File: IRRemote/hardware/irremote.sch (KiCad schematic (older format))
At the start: 35 parts, among them P1 USB_OTG, P2 TL1838_PINHEADER, P3 DS18B20_PINHEADER_TO92, P4 CONN_02X04, P5 CONN_01X04, P6 CONN_01X05, P7 CONN_01X04, P8 TEMP6000, P9 CONN_01X02, Q1 Q_NPN_BEC (MMBT2222ALT1G, 145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

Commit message: IRRemote layout
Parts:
- added R13, R14: 470, Resistors_SMD:R_0805_HandSoldering, symbol R
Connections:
- net RXD_UA_1: now also R14.2; no longer U1.22 (TXD)
- net TXD_UA_1: now also R13.2; no longer U1.21 (RXD)
- net USBDM_1- renamed USBDM_1_N
- net USBDP_1+ renamed USBDP_1_P
- new net: R13.1, U1.21 (RXD)
- new net: R14.1, U1.22 (TXD)
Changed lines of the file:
@@
 $EndComp
 $Comp
-L GND #PWR01
+L GND #PWR13
 U 1 1 58BC3861
 P 5550 4150
-F 0 "#PWR01" H 5550 3900 50  0001 C CNN
+F 0 "#PWR13" H 5550 3900 50  0001 C CNN
 F 1 "GND" H 5550 4000 50  0000 C CNN
 F 2 "" H 5550 4150 50  0000 C CNN
@@
 $EndComp
 $Comp
-L +3.3V #PWR02
+L +3.3V #PWR19
 U 1 1 58BC38AD
 P 6350 3600
-F 0 "#PWR02" H 6350 3450 50  0001 C CNN
+F 0 "#PWR19" H 6350 3450 50  0001 C CNN
 F 1 "+3.3V" H 6350 3740 50  0000 C CNN
 F 2 "" H 6350 3600 50  0000 C CNN
@@
 $EndComp
 $Comp
-L +5V #PWR03
+L +5V #PWR10
 U 1 1 58BC38D1
 P 4600 3600
-F 0 "#PWR03" H 4600 3450 50  0001 C CNN
+F 0 "#PWR10" H 4600 3450 50  0001 C CNN
 F 1 "+5V" H 4600 3740 50  0000 C CNN
 F 2 "" H 4600 3600 50  0000 C CNN
@@
 $EndComp
 $Comp
-L GND #PWR04
+L GND #PWR18
 U 1 1 58BC3BD7
 P 6300 5350
-F 0 "#PWR04" H 6300 5100 50  0001 C CNN
+F 0 "#PWR18" H 6300 5100 50  0001 C CNN
 F 1 "GND" H 6300 5200 50  0000 C CNN
 F 2 "" H 6300 5350 50  0000 C CNN
@@
 $EndComp
 $Comp
-L +5V #PWR05
+L +5V #PWR14
 U 1 1 58BC3BFA
 P 5650 5350
-F 0 "#PWR05" H 5650 5200 50  0001 C CNN
+F 0 "#PWR14" H 5650 5200 50  0001 C CNN
 F 1 "+5V" H 5650 5490 50  0000 C CNN
 F 2 "" H 5650 5350 50  0000 C CNN
@@
 $EndComp
 $Comp
-L GND #PWR06
+L GND #PWR9
 U 1 1 58BC3E12
 P 4550 2600
-F 0 "#PWR06" H 4550 2350 50  0001 C CNN
+F 0 "#PWR9" H 4550 2350 50  0001 C CNN
 F 1 "GND" H 4550 2450 50  0000 C CNN
 F 2 "" H 4550 2600 50  0000 C CNN
@@
 $EndComp
 $Comp
-L +3.3V #PWR07
+L +3.3V #PWR3
 U 1 1 58BC3E35
 P 2000 2500
-F 0 "#PWR07" H 2000 2350 50  0001 C CNN
+F 0 "#PWR3" H 2000 2350 50  0001 C CNN
 F 1 "+3.3V" H 2000 2640 50  0000 C CNN
 F 2 "" H 2000 2500 50  0000 C CNN
@@
 $EndComp
 $Comp
-L GND #PWR08
+L GND #PWR15
 U 1 1 58BC43F9
 P 5950 1700
-F 0 "#PWR08" H 5950 1450 50  0001 C CNN
+F 0 "#PWR15" H 5950 1450 50  0001 C CNN
 F 1 "GND" H 5950 1550 50  0000 C CNN
 F 2 "" H 5950 1700 50  0000 C CNN
@@
 $EndComp
 $Comp
-L +5V #PWR09
+L +5V #PWR24
 U 1 1 58BC455F
 P 7750 2200
-F 0 "#PWR09" H 7750 2050 50  0001 C CNN
+F 0 "#PWR24" H 7750 2050 50  0001 C CNN
 F 1 "+5V" H 7750 2340 50  0000 C CNN
 F 2 "" H 7750 2200 50  0000 C CNN
@@
 LED_DR
 $Comp
-L GND #PWR010
+L GND #PWR20
 U 1 1 58BC492A
 P 7300 3700
-F 0 "#PWR010" H 7300 3450 50  0001 C CNN
+F 0 "#PWR20" H 7300 3450 50  0001 C CNN
 F 1 "GND" H 7300 3550 50  0000 C CNN
 F 2 "" H 7300 3700 50  0000 C CNN
@@
 $EndComp
 $Comp
-L +3.3V #PWR011
+L +3.3V #PWR21
 U 1 1 58BC49D6
 P 7400 3550
-F 0 "#PWR011" H 7400 3400 50  0001 C CNN
+F 0 "#PWR21" H 7400 3400 50  0001 C CNN
 F 1 "+3.3V" H 7400 3690 50  0000 C CNN
 F 2 "" H 7400 3550 50  0000 C CNN
@@
 $EndComp
 $Comp
-L GND #PWR012
+L GND #PWR23
 U 1 1 58BC52F4
 P 7650 5200
-F 0 "#PWR012" H 7650 4950 50  0001 C CNN
+F 0 "#PWR23" H 7650 4950 50  0001 C CNN
 F 1 "GND" H 7650 5050 50  0000 C CNN
 F 2 "" H 7650 5200 50  0000 C CNN
@@
 $EndComp
 $Comp
-L +3.3V #PWR013
+L +3.3V #PWR22
 U 1 1 58BC52FA
 P 7650 4600
-F 0 "#PWR013" H 7650 4450 50  0001 C CNN
+F 0 "#PWR22" H 7650 4450 50  0001 C CNN
 F 1 "+3.3V" H 7650 4740 50  0000 C CNN
 F 2 "" H 7650 4600 50  0000 C CNN
@@
 $EndComp
 $Comp
-L GND #PWR014
+L GND #PWR6
 U 1 1 58C2C51A
 P 3600 5400
-F 0 "#PWR014" H 3600 5150 50  0001 C CNN
+F 0 "#PWR6" H 3600 5150 50  0001 C CNN
 F 1 "GND" H 3600 5250 50  0000 C CNN
 F 2 "" H 3600 5400 50  0000 C CNN
@@
 $EndComp
 Text GLabel 1400 5750 2    60   Input ~ 0
-USBDP_1+
+USBDP_1_P
 Text GLabel 3400 5800 0    60   Input ~ 0
-USBDM_1-
-$Comp
-L +5V #PWR015
+USBDM_1_N
+$Comp
+L +5V #PWR5
 U 1 1 58C2C51D
 P 3300 5250
-F 0 "#PWR015" H 3300 5100 50  0001 C CNN
+F 0 "#PWR5" H 3300 5100 50  0001 C CNN
 F 1 "+5V" H 3300 5390 50  0000 C CNN
 F 2 "" H 3300 5250 50  0000 C CNN
@@
 $EndComp
 $Comp
-L GND #PWR016
+L GND #PWR1
 U 1 1 58C2C51E
 P 1150 5250
-F 0 "#PWR016" H 1150 5000 50  0001 C CNN
+F 0 "#PWR1" H 1150 5000 50  0001 C CNN
 F 1 "GND" H 1150 5100 50  0000 C CNN
 F 2 "" H 1150 5250 50  0000 C CNN
@@
 $EndComp
 Text GLabel 6000 5700 2    60   Input ~ 0
-USBDP_1+
+USBDP_1_P
 Text GLabel 6000 5850 2    60   Input ~ 0
-USBDM_1-
+USBDM_1_N
 Text GLabel 1700 5150 0    60   Input ~ 0
 RXD_UA_1
-Text GLabel 4100 1450 1    60   Input ~ 0
+Text GLabel 4100 1000 1    60   Input ~ 0
 TXD_UA_1
-Text GLabel 4250 1450 1    60   Input ~ 0
+Text GLabel 4250 1000 1    60   Input ~ 0
 RXD_UA_1
 $Comp
@@
 $EndComp
 $Comp
-L +3.3V #PWR017
+L +3.3V #PWR8
 U 1 1 58C2D5B7
 P 4450 5150
-F 0 "#PWR017" H 4450 5000 50  0001 C CNN
+F 0 "#PWR8" H 4450 5000 50  0001 C CNN
 F 1 "+3.3V" H 4450 5290 50  0000 C CNN
 F 2 "" H 4450 5150 50  0000 C CNN
@@
 $EndComp
 $Comp
-L GND #PWR018
+L GND #PWR11
 U 1 1 58C2D60A
 P 4900 5150
-F 0 "#PWR018" H 4900 4900 50  0001 C CNN
+F 0 "#PWR11" H 4900 4900 50  0001 C CNN
 F 1 "GND" H 4900 5000 50  0000 C CNN
 F 2 "" H 4900 5150 50  0000 C CNN
@@
 $EndComp
 $Comp
-L +3.3V #PWR019
+L +3.3V #PWR2
 U 1 1 58C2E848
 P 1650 1600
-F 0 "#PWR019" H 1650 1450 50  0001 C CNN
+F 0 "#PWR2" H 1650 1450 50  0001 C CNN
 F 1 "+3.3V" H 1650 1740 50  0000 C CNN
 F 2 "" H 1650 1600 50  0000 C CNN
@@
 $EndComp
 $Comp
-L GND #PWR020
+L GND #PWR4
 U 1 1 58C2EADC
 P 2900 1050
-F 0 "#PWR020" H 2900 800 50  0001 C CNN
+F 0 "#PWR4" H 2900 800 50  0001 C CNN
 F 1 "GND" H 2900 900 50  0000 C CNN
 F 2 "" H 2900 1050 50  0000 C CNN
@@
 $EndComp
 $Comp
-L +3.3V #PWR021
+L +3.3V #PWR12
 U 1 1 58C2FF8D
 P 5300 2350
-F 0 "#PWR021" H 5300 2200 50  0001 C CNN
+F 0 "#PWR12" H 5300 2200 50  0001 C CNN
 F 1 "+3.3V" H 5300 2490 50  0000 C CNN
 F 2 "" H 5300 2350 50  0000 C CNN
@@
 $EndComp
 $Comp
-L GND #PWR022
+L GND #PWR7
 U 1 1 58C3055D
 P 4150 3250
-F 0 "#PWR022" H 4150 3000 50  0001 C CNN
+F 0 "#PWR7" H 4150 3000 50  0001 C CNN
 F 1 "GND" H 4150 3100 50  0000 C CNN
 F 2 "" H 4150 3250 50  0000 C CNN
@@
 $EndComp
 $Comp
-L GND #PWR023
+L GND #PWR16
 U 1 1 58C30AFA
 P 6150 2600
-F 0 "#PWR023" H 6150 2350 50  0001 C CNN
+F 0 "#PWR16" H 6150 2350 50  0001 C CNN
 F 1 "GND" H 6150 2450 50  0000 C CNN
 F 2 "" H 6150 2600 50  0000 C CNN
@@
 $EndComp
 $Comp
-L +3.3V #PWR024
+L +3.3V #PWR17
 U 1 1 58C30B00
 P 6250 2450
-F 0 "#PWR024" H 6250 2300 50  0001 C CNN
+F 0 "#PWR17" H 6250 2300 50  0001 C CNN
 F 1 "+3.3V" H 6250 2590 50  0000 C CNN
 F 2 "" H 6250 2450 50  0000 C CNN
@@
 $EndComp
 $Comp
-L GND #PWR025
+L GND #PWR26
 U 1 1 58C2E738
 P 8650 3950
-F 0 "#PWR025" H 8650 3700 50  0001 C CNN
+F 0 "#PWR26" H 8650 3700 50  0001 C CNN
 F 1 "GND" H 8650 3800 50  0000 C CNN
 F 2 "" H 8650 3950 50  0000 C CNN
@@
 $EndComp
 $Comp
-L +5V #PWR026
+L +5V #PWR25
 U 1 1 58C2E7AC
 P 8650 3650
-F 0 "#PWR026" H 8650 3500 50  0001 C CNN
+F 0 "#PWR25" H 8650 3500 50  0001 C CNN
 F 1 "+5V" H 8650 3790 50  0000 C CNN
 F 2 "" H 8650 3650 50  0000 C CNN
@@
 Wire Wire Line
 	8650 3750 8650 3650
+$Comp
+L R R13
+U 1 1 58C4A727
+P 4100 1300
+F 0 "R13" V 4180 1300 50  0000 C CNN
+F 1 "470" V 4100 1300 50  0000 C CNN
+F 2 "Resistors_SMD:R_0805_HandSoldering" V 4030 1300 50  0001 C CNN
+F 3 "" H 4100 1300 50  0000 C CNN
+	1    4100 1300
+	-1   0    0    1
+$EndComp
+$Comp
+L R R14
+U 1 1 58C4A7E7
+P 4250 1300
+F 0 "R14" V 4330 1300 50  0000 C CNN
+F 1 "470" V 4250 1300 50  0000 C CNN
+F 2 "Resistors_SMD:R_0805_HandSoldering" V 4180 1300 50  0001 C CNN
+F 3 "" H 4250 1300 50  0000 C CNN
+	1    4250 1300
+	-1   0    0    1
+$EndComp
+Wire Wire Line
+	4250 1000 4250 1150
+Wire Wire Line
+	4100 1150 4100 1000
 $EndSCHEMATC

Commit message: removed the uart and made the board smaller
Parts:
- removed C5: C, Capacitors_SMD:C_0805_HandSoldering, symbol C
- removed P1: USB_OTG, MyKiCadLibs:USB_Micro-B-OshPark, symbol USB_OTG
- removed R13, R14: 470, Resistors_SMD:R_0805_HandSoldering, symbol R
- removed R6, R7: 27, Resistors_SMD:R_0805_HandSoldering, symbol R
- removed U3: FT230XS, Housings_SSOP:SSOP-16_3.9x4.9mm_Pitch0.635mm, symbol FT230XS
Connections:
- net RXD_UA_1: now also U1.22 (TXD)
- net TXD_UA_1: now also U1.21 (RXD)

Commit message: updated board for correct SMD push buttons
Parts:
- SW1, SW2: footprint Buttons_Switches_SMD:SW_SPST_EVQPE1 -> Buttons_Switches_SMD:SW_SPST_FSMSM
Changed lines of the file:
@@
 F 0 "SW1" H 2650 1160 50  0000 C CNN
 F 1 "SW_PUSH" H 2500 970 50  0000 C CNN
-F 2 "Buttons_Switches_SMD:SW_SPST_EVQPE1" H 2500 1050 50  0001 C CNN
+F 2 "Buttons_Switches_SMD:SW_SPST_FSMSM" H 2500 1050 50  0001 C CNN
 F 3 "" H 2500 1050 50  0000 C CNN
 	1    2500 1050
@@
 F 0 "SW2" H 4200 2960 50  0000 C CNN
 F 1 "SW_PUSH" H 4050 2770 50  0000 C CNN
-F 2 "Buttons_Switches_SMD:SW_SPST_EVQPE1" H 4050 2850 50  0001 C CNN
+F 2 "Buttons_Switches_SMD:SW_SPST_FSMSM" H 4050 2850 50  0001 C CNN
 F 3 "" H 4050 2850 50  0000 C CNN
 	1    4050 2850

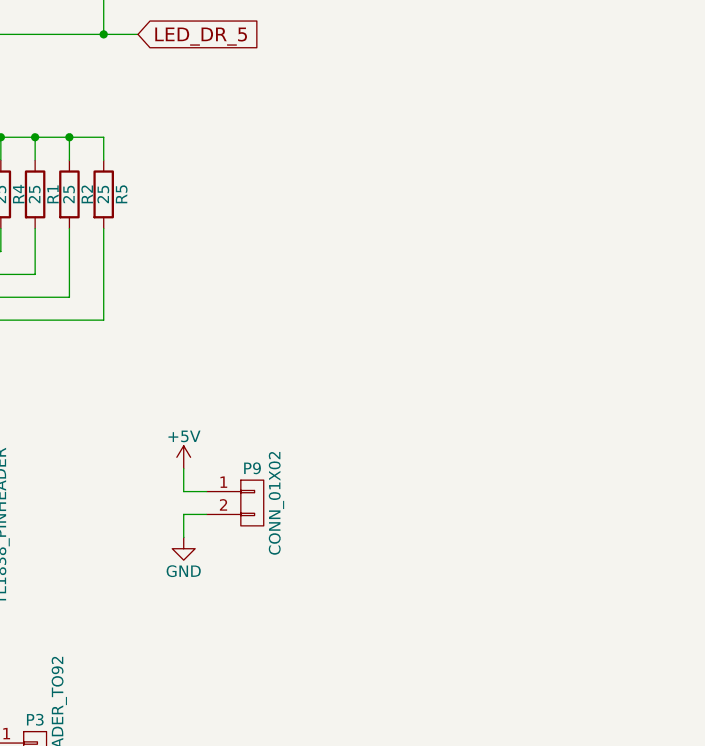
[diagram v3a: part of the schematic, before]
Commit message: moved the microusb for power, fixed push button switches, flipped IR receiver
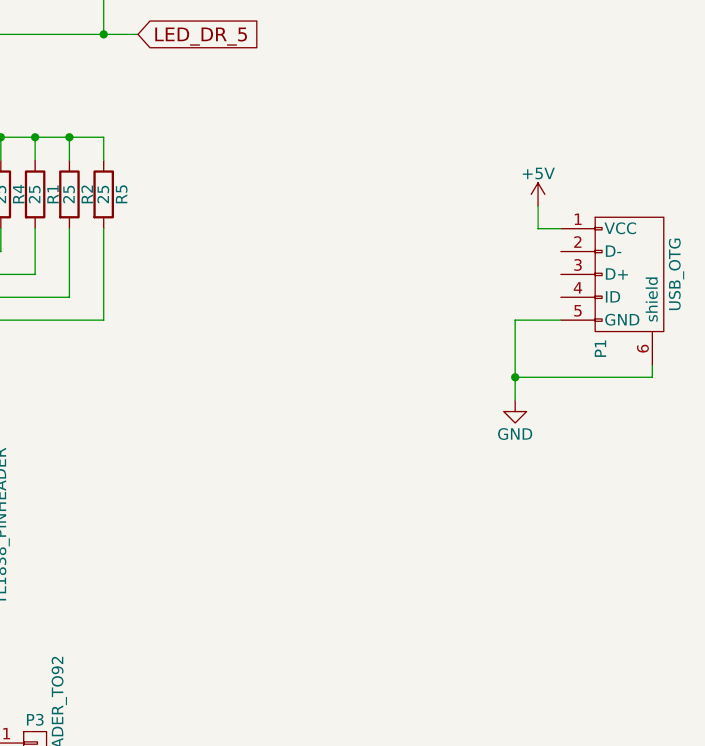
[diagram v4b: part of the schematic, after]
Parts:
- removed P9: CONN_01X02, Pin_Headers:Pin_Header_Straight_1x02, symbol CONN_01X02
- added P1: USB_OTG, MyKiCadLibs:USB_Micro-B-OshPark, symbol USB_OTG
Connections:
- net +5V: now also P1.1 (VCC)
- net GND: now also P1.5 (GND), P1.6 (shield)
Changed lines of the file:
@@
 $EndComp
 $Comp
-L GND #PWR01
+L GND #PWR10
 U 1 1 58BC3861
 P 5550 4150
-F 0 "#PWR01" H 5550 3900 50  0001 C CNN
+F 0 "#PWR10" H 5550 3900 50  0001 C CNN
 F 1 "GND" H 5550 4000 50  0000 C CNN
 F 2 "" H 5550 4150 50  0000 C CNN
@@
 $EndComp
 $Comp
-L +3.3V #PWR02
+L +3.3V #PWR14
 U 1 1 58BC38AD
 P 6350 3600
-F 0 "#PWR02" H 6350 3450 50  0001 C CNN
+F 0 "#PWR14" H 6350 3450 50  0001 C CNN
 F 1 "+3.3V" H 6350 3740 50  0000 C CNN
 F 2 "" H 6350 3600 50  0000 C CNN
@@
 $EndComp
 $Comp
-L +5V #PWR03
+L +5V #PWR7
 U 1 1 58BC38D1
 P 4600 3600
-F 0 "#PWR03" H 4600 3450 50  0001 C CNN
+F 0 "#PWR7" H 4600 3450 50  0001 C CNN
 F 1 "+5V" H 4600 3740 50  0000 C CNN
 F 2 "" H 4600 3600 50  0000 C CNN
@@
 $EndComp
 $Comp
-L GND #PWR04
+L GND #PWR6
 U 1 1 58BC3E12
 P 4550 2600
-F 0 "#PWR04" H 4550 2350 50  0001 C CNN
+F 0 "#PWR6" H 4550 2350 50  0001 C CNN
 F 1 "GND" H 4550 2450 50  0000 C CNN
 F 2 "" H 4550 2600 50  0000 C CNN
@@
 $EndComp
 $Comp
-L +3.3V #PWR05
+L +3.3V #PWR2
 U 1 1 58BC3E35
 P 2000 2500
-F 0 "#PWR05" H 2000 2350 50  0001 C CNN
+F 0 "#PWR2" H 2000 2350 50  0001 C CNN
 F 1 "+3.3V" H 2000 2640 50  0000 C CNN
 F 2 "" H 2000 2500 50  0000 C CNN
@@
 $EndComp
 $Comp
-L GND #PWR06
+L GND #PWR11
 U 1 1 58BC43F9
 P 5950 1700
-F 0 "#PWR06" H 5950 1450 50  0001 C CNN
+F 0 "#PWR11" H 5950 1450 50  0001 C CNN
 F 1 "GND" H 5950 1550 50  0000 C CNN
 F 2 "" H 5950 1700 50  0000 C CNN
@@
 $EndComp
 $Comp
-L +5V #PWR07
+L +5V #PWR19
 U 1 1 58BC455F
 P 7750 2200
-F 0 "#PWR07" H 7750 2050 50  0001 C CNN
+F 0 "#PWR19" H 7750 2050 50  0001 C CNN
 F 1 "+5V" H 7750 2340 50  0000 C CNN
 F 2 "" H 7750 2200 50  0000 C CNN
@@
 LED_DR
 $Comp
-L GND #PWR08
+L GND #PWR15
 U 1 1 58BC492A
 P 7300 3700
-F 0 "#PWR08" H 7300 3450 50  0001 C CNN
+F 0 "#PWR15" H 7300 3450 50  0001 C CNN
 F 1 "GND" H 7300 3550 50  0000 C CNN
 F 2 "" H 7300 3700 50  0000 C CNN
@@
 $EndComp
 $Comp
-L +3.3V #PWR09
+L +3.3V #PWR16
 U 1 1 58BC49D6
 P 7400 3550
-F 0 "#PWR09" H 7400 3400 50  0001 C CNN
+F 0 "#PWR16" H 7400 3400 50  0001 C CNN
 F 1 "+3.3V" H 7400 3690 50  0000 C CNN
 F 2 "" H 7400 3550 50  0000 C CNN
@@
 $EndComp
 $Comp
-L GND #PWR010
+L GND #PWR18
 U 1 1 58BC52F4
 P 7650 5200
-F 0 "#PWR010" H 7650 4950 50  0001 C CNN
+F 0 "#PWR18" H 7650 4950 50  0001 C CNN
 F 1 "GND" H 7650 5050 50  0000 C CNN
 F 2 "" H 7650 5200 50  0000 C CNN
@@
 $EndComp
 $Comp
-L +3.3V #PWR011
+L +3.3V #PWR17
 U 1 1 58BC52FA
 P 7650 4600
-F 0 "#PWR011" H 7650 4450 50  0001 C CNN
+F 0 "#PWR17" H 7650 4450 50  0001 C CNN
 F 1 "+3.3V" H 7650 4740 50  0000 C CNN
 F 2 "" H 7650 4600 50  0000 C CNN
@@
 $EndComp
 $Comp
-L +3.3V #PWR012
+L +3.3V #PWR5
 U 1 1 58C2D5B7
 P 4450 5150
-F 0 "#PWR012" H 4450 5000 50  0001 C CNN
+F 0 "#PWR5" H 4450 5000 50  0001 C CNN
 F 1 "+3.3V" H 4450 5290 50  0000 C CNN
 F 2 "" H 4450 5150 50  0000 C CNN
@@
 $EndComp
 $Comp
-L GND #PWR013
+L GND #PWR8
 U 1 1 58C2D60A
 P 4900 5150
-F 0 "#PWR013" H 4900 4900 50  0001 C CNN
+F 0 "#PWR8" H 4900 4900 50  0001 C CNN
 F 1 "GND" H 4900 5000 50  0000 C CNN
 F 2 "" H 4900 5150 50  0000 C CNN
@@
 $EndComp
 $Comp
-L +3.3V #PWR014
+L +3.3V #PWR1
 U 1 1 58C2E848
 P 1650 1600
-F 0 "#PWR014" H 1650 1450 50  0001 C CNN
+F 0 "#PWR1" H 1650 1450 50  0001 C CNN
 F 1 "+3.3V" H 1650 1740 50  0000 C CNN
 F 2 "" H 1650 1600 50  0000 C CNN
@@
 $EndComp
 $Comp
-L GND #PWR015
+L GND #PWR3
 U 1 1 58C2EADC
 P 2900 1050
-F 0 "#PWR015" H 2900 800 50  0001 C CNN
+F 0 "#PWR3" H 2900 800 50  0001 C CNN
 F 1 "GND" H 2900 900 50  0000 C CNN
 F 2 "" H 2900 1050 50  0000 C CNN
@@
 $EndComp
 $Comp
-L +3.3V #PWR016
+L +3.3V #PWR9
 U 1 1 58C2FF8D
 P 5300 2350
-F 0 "#PWR016" H 5300 2200 50  0001 C CNN
+F 0 "#PWR9" H 5300 2200 50  0001 C CNN
 F 1 "+3.3V" H 5300 2490 50  0000 C CNN
 F 2 "" H 5300 2350 50  0000 C CNN
@@
 $EndComp
 $Comp
-L GND #PWR017
+L GND #PWR4
 U 1 1 58C3055D
 P 4150 3250
-F 0 "#PWR017" H 4150 3000 50  0001 C CNN
+F 0 "#PWR4" H 4150 3000 50  0001 C CNN
 F 1 "GND" H 4150 3100 50  0000 C CNN
 F 2 "" H 4150 3250 50  0000 C CNN
@@
 $EndComp
 $Comp
-L GND #PWR018
+L GND #PWR12
 U 1 1 58C30AFA
 P 6150 2600
-F 0 "#PWR018" H 6150 2350 50  0001 C CNN
+F 0 "#PWR12" H 6150 2350 50  0001 C CNN
 F 1 "GND" H 6150 2450 50  0000 C CNN
 F 2 "" H 6150 2600 50  0000 C CNN
@@
 $EndComp
 $Comp
-L +3.3V #PWR019
+L +3.3V #PWR13
 U 1 1 58C30B00
 P 6250 2450
-F 0 "#PWR019" H 6250 2300 50  0001 C CNN
+F 0 "#PWR13" H 6250 2300 50  0001 C CNN
 F 1 "+3.3V" H 6250 2590 50  0000 C CNN
 F 2 "" H 6250 2450 50  0000 C CNN
@@
 	2100 2900 2100 3250
 $Comp
-L CONN_01X02 P9
-U 1 1 58C2E676
-P 8950 3800
-F 0 "P9" H 8950 3950 50  0000 C CNN
-F 1 "CONN_01X02" V 9050 3800 50  0000 C CNN
-F 2 "Pin_Headers:Pin_Header_Straight_1x02" H 8950 3800 50  0001 C CNN
-F 3 "" H 8950 3800 50  0000 C CNN
-	1    8950 3800
-	1    0    0    -1
-$EndComp
-$Comp
-L GND #PWR020
+L GND #PWR20
 U 1 1 58C2E738
-P 8650 3950
-F 0 "#PWR020" H 8650 3700 50  0001 C CNN
-F 1 "GND" H 8650 3800 50  0000 C CNN
-F 2 "" H 8650 3950 50  0000 C CNN
-F 3 "" H 8650 3950 50  0000 C CNN
-	1    8650 3950
-	1    0    0    -1
-$EndComp
-$Comp
-L +5V #PWR021
+P 10100 3350
+F 0 "#PWR20" H 10100 3100 50  0001 C CNN
+F 1 "GND" H 10100 3200 50  0000 C CNN
+F 2 "" H 10100 3350 50  0000 C CNN
+F 3 "" H 10100 3350 50  0000 C CNN
+	1    10100 3350
+	1    0    0    -1
+$EndComp
+$Comp
+L +5V #PWR21
 U 1 1 58C2E7AC
-P 8650 3650
-F 0 "#PWR021" H 8650 3500 50  0001 C CNN
-F 1 "+5V" H 8650 3790 50  0000 C CNN
-F 2 "" H 8650 3650 50  0000 C CNN
-F 3 "" H 8650 3650 50  0000 C CNN
-	1    8650 3650
-	1    0    0    -1
-$EndComp
-Wire Wire Line
-	8650 3950 8650 3850
-Wire Wire Line
-	8650 3850 8750 3850
-Wire Wire Line
-	8750 3750 8650 3750
-Wire Wire Line
-	8650 3750 8650 3650
+P 10200 2500
+F 0 "#PWR21" H 10200 2350 50  0001 C CNN
+F 1 "+5V" H 10200 2640 50  0000 C CNN
+F 2 "" H 10200 2500 50  0000 C CNN
+F 3 "" H 10200 2500 50  0000 C CNN
+	1    10200 2500
+	1    0    0    -1
+$EndComp
+Wire Wire Line
+	10300 2600 10200 2600
+Wire Wire Line
+	10200 2600 10200 2500
+$Comp
+L USB_OTG P1
+U 1 1 58E5A42E
+P 10600 2800
+F 0 "P1" H 10925 2675 50  0000 C CNN
+F 1 "USB_OTG" H 10600 3000 50  0000 C CNN
+F 2 "MyKiCadLibs:USB_Micro-B-OshPark" V 10550 2700 50  0001 C CNN
+F 3 "" V 10550 2700 50  0000 C CNN
+	1    10600 2800
+	0    1    1    0
+$EndComp
+Wire Wire Line
+	10300 3000 10100 3000
+Wire Wire Line
+	10100 3000 10100 3350
+Wire Wire Line
+	10700 3200 10700 3250
+Wire Wire Line
+	10700 3250 10100 3250
+Connection ~ 10100 3250
 $EndSCHEMATC

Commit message: new multi-sensor
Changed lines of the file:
@@
 $EndComp
 $Comp
-L GND #PWR10
+L GND #PWR01
 U 1 1 58BC3861
 P 5550 4150
-F 0 "#PWR10" H 5550 3900 50  0001 C CNN
+F 0 "#PWR01" H 5550 3900 50  0001 C CNN
 F 1 "GND" H 5550 4000 50  0000 C CNN
 F 2 "" H 5550 4150 50  0000 C CNN
@@
 $EndComp
 $Comp
-L +3.3V #PWR14
+L +3.3V #PWR02
 U 1 1 58BC38AD
 P 6350 3600
-F 0 "#PWR14" H 6350 3450 50  0001 C CNN
+F 0 "#PWR02" H 6350 3450 50  0001 C CNN
 F 1 "+3.3V" H 6350 3740 50  0000 C CNN
 F 2 "" H 6350 3600 50  0000 C CNN
@@
 $EndComp
 $Comp
-L +5V #PWR7
+L +5V #PWR03
 U 1 1 58BC38D1
 P 4600 3600
-F 0 "#PWR7" H 4600 3450 50  0001 C CNN
+F 0 "#PWR03" H 4600 3450 50  0001 C CNN
 F 1 "+5V" H 4600 3740 50  0000 C CNN
 F 2 "" H 4600 3600 50  0000 C CNN
@@
 $EndComp
 $Comp
-L GND #PWR6
+L GND #PWR04
 U 1 1 58BC3E12
 P 4550 2600
-F 0 "#PWR6" H 4550 2350 50  0001 C CNN
+F 0 "#PWR04" H 4550 2350 50  0001 C CNN
 F 1 "GND" H 4550 2450 50  0000 C CNN
 F 2 "" H 4550 2600 50  0000 C CNN
@@
 $EndComp
 $Comp
-L +3.3V #PWR2
+L +3.3V #PWR05
 U 1 1 58BC3E35
 P 2000 2500
-F 0 "#PWR2" H 2000 2350 50  0001 C CNN
+F 0 "#PWR05" H 2000 2350 50  0001 C CNN
 F 1 "+3.3V" H 2000 2640 50  0000 C CNN
 F 2 "" H 2000 2500 50  0000 C CNN
@@
 $EndComp
 $Comp
-L GND #PWR11
+L GND #PWR06
 U 1 1 58BC43F9
 P 5950 1700
-F 0 "#PWR11" H 5950 1450 50  0001 C CNN
+F 0 "#PWR06" H 5950 1450 50  0001 C CNN
 F 1 "GND" H 5950 1550 50  0000 C CNN
 F 2 "" H 5950 1700 50  0000 C CNN
@@
 $EndComp
 $Comp
-L +5V #PWR19
+L +5V #PWR07
 U 1 1 58BC455F
 P 7750 2200
-F 0 "#PWR19" H 7750 2050 50  0001 C CNN
+F 0 "#PWR07" H 7750 2050 50  0001 C CNN
 F 1 "+5V" H 7750 2340 50  0000 C CNN
 F 2 "" H 7750 2200 50  0000 C CNN
@@
 LED_DR
 $Comp
-L GND #PWR15
+L GND #PWR08
 U 1 1 58BC492A
 P 7300 3700
-F 0 "#PWR15" H 7300 3450 50  0001 C CNN
+F 0 "#PWR08" H 7300 3450 50  0001 C CNN
 F 1 "GND" H 7300 3550 50  0000 C CNN
 F 2 "" H 7300 3700 50  0000 C CNN
@@
 $EndComp
 $Comp
-L +3.3V #PWR16
+L +3.3V #PWR09
 U 1 1 58BC49D6
 P 7400 3550
-F 0 "#PWR16" H 7400 3400 50  0001 C CNN
+F 0 "#PWR09" H 7400 3400 50  0001 C CNN
 F 1 "+3.3V" H 7400 3690 50  0000 C CNN
 F 2 "" H 7400 3550 50  0000 C CNN
@@
 $EndComp
 $Comp
-L GND #PWR18
+L GND #PWR010
 U 1 1 58BC52F4
 P 7650 5200
-F 0 "#PWR18" H 7650 4950 50  0001 C CNN
+F 0 "#PWR010" H 7650 4950 50  0001 C CNN
 F 1 "GND" H 7650 5050 50  0000 C CNN
 F 2 "" H 7650 5200 50  0000 C CNN
@@
 $EndComp
 $Comp
-L +3.3V #PWR17
+L +3.3V #PWR011
 U 1 1 58BC52FA
 P 7650 4600
-F 0 "#PWR17" H 7650 4450 50  0001 C CNN
+F 0 "#PWR011" H 7650 4450 50  0001 C CNN
 F 1 "+3.3V" H 7650 4740 50  0000 C CNN
 F 2 "" H 7650 4600 50  0000 C CNN
@@
 $EndComp
 $Comp
-L +3.3V #PWR5
+L +3.3V #PWR012
 U 1 1 58C2D5B7
 P 4450 5150
-F 0 "#PWR5" H 4450 5000 50  0001 C CNN
+F 0 "#PWR012" H 4450 5000 50  0001 C CNN
 F 1 "+3.3V" H 4450 5290 50  0000 C CNN
 F 2 "" H 4450 5150 50  0000 C CNN
@@
 $EndComp
 $Comp
-L GND #PWR8
+L GND #PWR013
 U 1 1 58C2D60A
 P 4900 5150
-F 0 "#PWR8" H 4900 4900 50  0001 C CNN
+F 0 "#PWR013" H 4900 4900 50  0001 C CNN
 F 1 "GND" H 4900 5000 50  0000 C CNN
 F 2 "" H 4900 5150 50  0000 C CNN
@@
 $EndComp
 $Comp
-L +3.3V #PWR1
+L +3.3V #PWR014
 U 1 1 58C2E848
 P 1650 1600
-F 0 "#PWR1" H 1650 1450 50  0001 C CNN
+F 0 "#PWR014" H 1650 1450 50  0001 C CNN
 F 1 "+3.3V" H 1650 1740 50  0000 C CNN
 F 2 "" H 1650 1600 50  0000 C CNN
@@
 $EndComp
 $Comp
-L GND #PWR3
+L GND #PWR015
 U 1 1 58C2EADC
 P 2900 1050
-F 0 "#PWR3" H 2900 800 50  0001 C CNN
+F 0 "#PWR015" H 2900 800 50  0001 C CNN
 F 1 "GND" H 2900 900 50  0000 C CNN
 F 2 "" H 2900 1050 50  0000 C CNN
@@
 $EndComp
 $Comp
-L +3.3V #PWR9
+L +3.3V #PWR016
 U 1 1 58C2FF8D
 P 5300 2350
-F 0 "#PWR9" H 5300 2200 50  0001 C CNN
+F 0 "#PWR016" H 5300 2200 50  0001 C CNN
 F 1 "+3.3V" H 5300 2490 50  0000 C CNN
 F 2 "" H 5300 2350 50  0000 C CNN
@@
 $EndComp
 $Comp
-L GND #PWR4
+L GND #PWR017
 U 1 1 58C3055D
 P 4150 3250
-F 0 "#PWR4" H 4150 3000 50  0001 C CNN
+F 0 "#PWR017" H 4150 3000 50  0001 C CNN
 F 1 "GND" H 4150 3100 50  0000 C CNN
 F 2 "" H 4150 3250 50  0000 C CNN
@@
 $EndComp
 $Comp
-L GND #PWR12
+L GND #PWR018
 U 1 1 58C30AFA
 P 6150 2600
-F 0 "#PWR12" H 6150 2350 50  0001 C CNN
+F 0 "#PWR018" H 6150 2350 50  0001 C CNN
 F 1 "GND" H 6150 2450 50  0000 C CNN
 F 2 "" H 6150 2600 50  0000 C CNN
@@
 $EndComp
 $Comp
-L +3.3V #PWR13
+L +3.3V #PWR019
 U 1 1 58C30B00
 P 6250 2450
-F 0 "#PWR13" H 6250 2300 50  0001 C CNN
+F 0 "#PWR019" H 6250 2300 50  0001 C CNN
 F 1 "+3.3V" H 6250 2590 50  0000 C CNN
 F 2 "" H 6250 2450 50  0000 C CNN
@@
 Connection ~ 8300 1750
 Wire Wire Line
-	10850 9450 10750 9450
-Wire Wire Line
 	4250 1700 4000 1700
 Wire Wire Line
@@
 	2100 2900 2100 3250
 $Comp
-L GND #PWR20
+L GND #PWR020
 U 1 1 58C2E738
 P 10100 3350
-F 0 "#PWR20" H 10100 3100 50  0001 C CNN
+F 0 "#PWR020" H 10100 3100 50  0001 C CNN
 F 1 "GND" H 10100 3200 50  0000 C CNN
 F 2 "" H 10100 3350 50  0000 C CNN
@@
 $EndComp
 $Comp
-L +5V #PWR21
+L +5V #PWR021
 U 1 1 58C2E7AC
 P 10200 2500
-F 0 "#PWR21" H 10200 2350 50  0001 C CNN
+F 0 "#PWR021" H 10200 2350 50  0001 C CNN
 F 1 "+5V" H 10200 2640 50  0000 C CNN
 F 2 "" H 10200 2500 50  0000 C CNN
